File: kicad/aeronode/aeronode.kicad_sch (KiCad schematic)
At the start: 38 parts, among them J1 IMU_BOARD, J2 USB-C PD / recovery, J3 2S LiFePO4 6Ah + BMS, Q1 NMOS pass - TBD, U1 ConnectCore93_LGA, U2 CYPD3177-24LQ, U3 BQ25798, U4 LMR33630ADDA, U5 LTC4364CMS

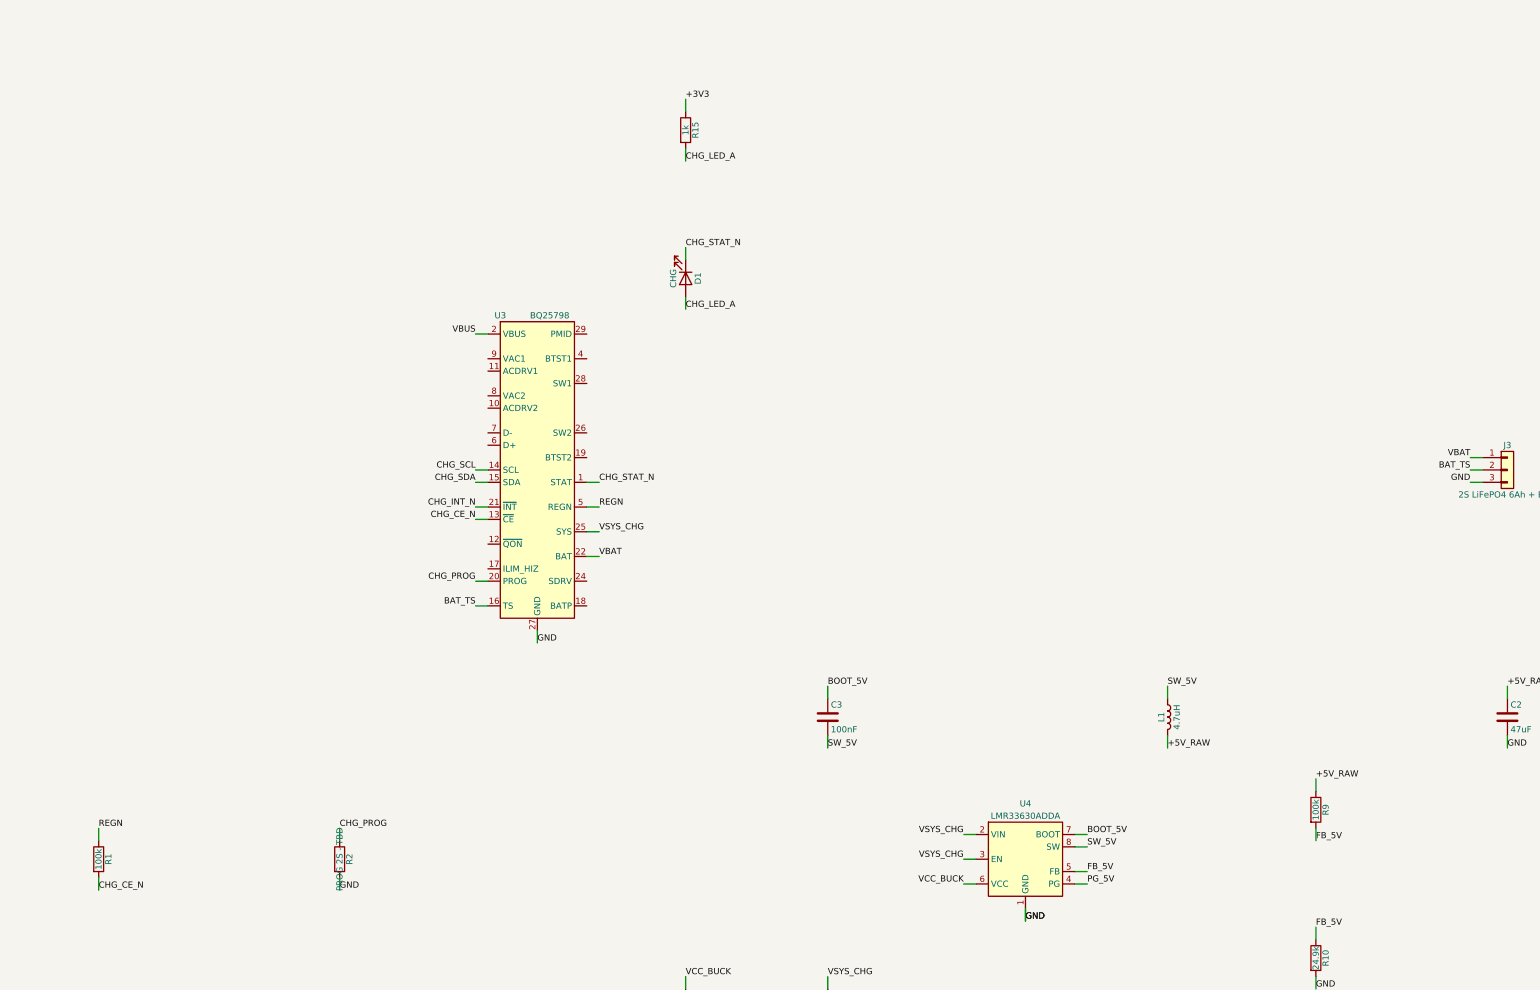
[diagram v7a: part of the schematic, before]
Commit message: [LIMA] aeronode: BQ25798 power stage and TS network; TS values are Li-ion, not LFP
All values from the datasheet's application diagram and Table 7-1:

  R2   6.04k   PROG - Table 7-1 gives POR 1.5MHz / 2s. Was TBD
  L2   1.0uH   buck-boost inductor SW1-SW2 (1.0uH pairs with 1.5MHz)
  C6/C7 47nF   bootstraps
  C8   4.7uF   REGN
  C9-C12 10uF  VBUS, PMID, BAT, SYS bulk
  R23/R24 5.24k/30.31k  TS divider REGN-TS-GND

Table 7-1 also confirms an assumption I had been carrying rather than checking:
2s POR defaults are ICHG 1A, VSYSMIN 7V, VREG 8.4V, VREG range 5-9.99V. That
7V VSYSMIN is exactly what puts SYS at 7.0-7.3V, which is why the buck and the
OVP exist at all. 7.20V sits comfortably inside the allowed VREG range.

WARNING recorded: R23/R24 are the datasheet's LI-ION values, derived for
T1=0C and T5=60C. LiFePO4 does not charge to 60C - its window is about 0-45C -
so as placed the hardware would permit charging outside the pack's safe range.
Fix before fab by recomputing the divider for 0/45C using the datasheet's
equations, or by tightening the JEITA thresholds over I2C.

That is the THIRD Li-ion default to bite this design after the 8.4V VREG and the
watchdog revert. The pattern is consistent enough to state plainly: every
chemistry-dependent default on this charger assumes Li-ion and should be treated
as wrong until checked.

Verified: all ten charger power-stage nets matched predicted endpoint counts.
ERC 182, no isolated labels, no pin_to_pin. The 5 power_pin_not_driven are
missing PWR_FLAGs, noted for the tidy-up.
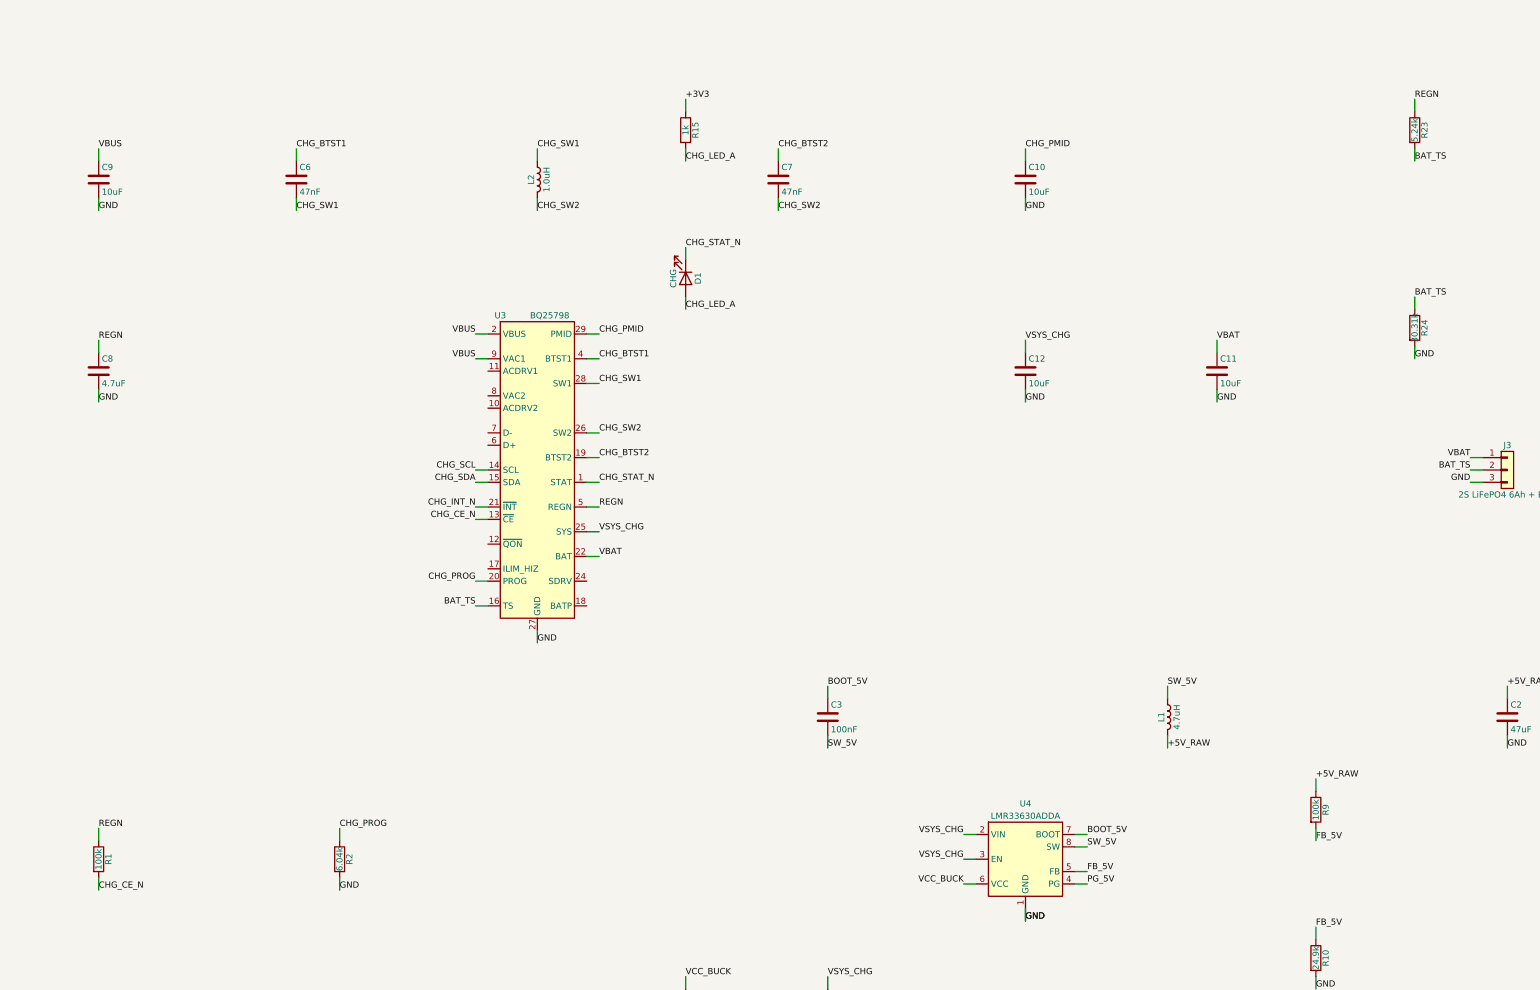
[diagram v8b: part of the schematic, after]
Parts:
- added C10, C11, C12, C9: 10uF, symbol Device:C
- added C6, C7: 47nF, symbol Device:C
- added C8: 4.7uF, symbol Device:C
- added L2: 1.0uH, symbol Device:L
- added R23: 5.24k, symbol Device:R
- added R24: 30.31k, symbol Device:R
- R2: value PROG 2S - TBD -> 6.04k
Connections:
- net BAT_TS: now also R23.2, R24.1
- net GND: now also C10.2, C11.2, C12.2, C8.2, C9.2, R24.2
- net REGN: now also C8.1, R23.1
- net VBAT: now also C11.1
- net VBUS: now also U3.9 (VAC1), C9.1
- net VSYS_CHG: now also C12.1
- net CHG_BTST2: now reaches U3.19 (BTST2)
- net CHG_BTST2: now also C7.1
- net CHG_SW2: now reaches U3.26 (SW2)
- net CHG_SW2: now also C7.2, L2.2
- net CHG_SW1: now reaches U3.28 (SW1)
- net CHG_SW1: now also C6.2, L2.1
- net CHG_PMID: now reaches U3.29 (PMID)
- net CHG_PMID: now also C10.1
- net CHG_BTST1: now reaches U3.4 (BTST1)
- net CHG_BTST1: now also C6.1
